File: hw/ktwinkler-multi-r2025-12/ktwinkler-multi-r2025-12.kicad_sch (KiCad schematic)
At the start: 21 parts, among them J1 USB_C_Receptacle_USB2.0_16P, J2 Conn_01x03, J3 Conn_01x03, J4 Conn_01x01, J5 Conn_01x01, SW5 MODE, U1 TPS631000DRLR, U2 LK116, U3 ESP32-C3FH4, Y1 40M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

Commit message: make a v2 idea, mroe experiments, less product...
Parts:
- removed AE1: Antenna_Dipole, symbol Device:Antenna_Dipole
- removed C1, C2, C3, C4, C5: 100nF, Capacitor_SMD:C_0603_1608Metric, symbol karl-atomic-basic:KC0603_100nF
- removed J1: USB_C_Receptacle_USB2.0_16P, Connector_USB:USB_C_Receptacle_GCT_USB4110, symbol Connector:USB_C_Receptacle_USB2.0_16P
- removed J2: Conn_01x03, Connector_PinHeader_2.54mm:PinHeader_1x03_P2.54mm_Vertical, symbol Connector_Generic:Conn_01x03
- removed J3: Conn_01x03, TerminalBlock_Phoenix_MPT-0,5-3-2.54_1x03_P2.54mm_Horizontal, symbol Connector_Generic:Conn_01x03
- removed J4, J5: Conn_01x01, Connector_Wire:SolderWire-0.5sqmm_1x01_D0.9mm_OD2.1mm, symbol Connector_Generic:Conn_01x01
- removed L1: 1uH, Inductor_SMD:L_1206_3216Metric, symbol Device:L_Small
- removed R1, R2: 5k1, Resistor_SMD:R_0603_1608Metric, symbol karl-atomic-basic:KR0603_5k1
- removed R3: 0R, Resistor_SMD:R_0603_1608Metric, symbol karl-atomic-basic:KR0603_0R
- removed U1: TPS631000DRLR, Package_TO_SOT_SMD:SOT-583-8, symbol karl-parts:TPS631000DRLR
- removed U2: LK116, Package_TO_SOT_SMD:SOT-23-6, symbol karl-parts:LK116
- removed U3: ESP32-C3FH4, Package_DFN_QFN:QFN-32-1EP_5x5mm_P0.5mm_EP3.7x3.7mm, symbol karl-parts:ESP32-C3FH4
- removed Y1: 40M, Crystal:Crystal_SMD_2016-4Pin_2.0x1.6mm, symbol Device:Crystal_GND24_Small
- removed Y2: X1A0001210005, Crystal:Crystal_SMD_MicroCrystal_CM9V-T1A-2Pin_1.6x1.0mm, symbol karl-parts:X1A0001210005
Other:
- added sheet esp32 (esp32.kicad_sch)
- added sheet leds (leds.kicad_sch)
- added sheet power (power.kicad_sch)
- note removed: "2/3 cells AA, with shitty 1.2V nimh, flat, we need buck boost from ~2V to ~4.6V Decent parts on JLC, under $0.60, with >1A RT6150A (0.8A, 1MHz) TPS63802DLAR 3A, promises 0.47uH tiny L TPS63020 4A, 2.4MHz (bigger package) TPS631000 (great stock, looks good)"
- note removed: "2016 is the cheapest smallest 40M crystal if you do this yourself the hard way Do we _realllllly_ need a 32k? yeahhhh, that's the point right?"
- note removed: "Constraints * Only the one user facing button from external * Updates? * Programming? USB-C inside? just serial pads?"
- note removed: "ESP32x in 13.2x16.6mm modules: ESP32-C6-MINI-1-N4 - well stocked, $4 (wifi+btle+802.15.4) ESP32-C61-MINI-1 - no stock ESP32-C3-MINI-1-H4X - well stocked, $3 (wifi+btle) ESP8684-MINI-1-H4 - some stock, $2 (wifi+btle) ESP32-H2-MINI-1 - no stock (btle+802.15.4 only) ESP32-PICO-MINI-02-N8R2 - well stocked, $5 (wifi+bt+btle) So... C6 or C3? fuck matter... C3 is fine :) So.. C6 has the low power coproc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"
- note removed: "Separate because these are battery contacts in the replacement board"
- note removed: "TODO: use 0402 TODO: will a vert mount fit? (prb too tall?)"
- note removed: "This controller _will_ drain the batteries when "off"! Original parts use ~370nA when "off" we'll never get that low!"
- note removed: "battery: Keystone 5201 is spring, would need bending and insertion. one of my boards is positive on left pin, one is negative.... Keystone 5223 is the other side. (on lcsc, but not good for straigth soldering!) Holes for mounting: they're in different places Buttons: different offsets and different sides!"
- note removed: "~4V, peak power is.... what? 0.4 2W? Connect the boards up again?"
- moved on the sheet: SW5

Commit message: pushing onwards like a madlad
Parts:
- added R14: 10k, Resistor_SMD:R_0402_1005Metric, symbol karl-atomic-basic:KR0402_10k
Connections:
- net GND: now reaches SW5.1
- net MODE: now reaches SW5.2
- net MODE: now also R14.2
- new net +3V3: R14.1
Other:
- added sheet ch584 (ch584.kicad_sch)
- sheet esp32 ports: added MODE, PWM1, PWM2, PWM3, PWM4, PWM5, PWM6, PWM7, PWM8; removed none
- sheet leds ports: added LED1A, LED1B, LED2A, LED2B, LED3A, LED3B, LED4A, LED4B, PWR_LEDS; removed none
- note added: "Not enough PWM on CH584F ;)"
- moved on the sheet: SW5

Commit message: ready for scope creep
I think the schematic is ... mostly ok?  I need to decide how much of
the han p1 port scope creep to bother doing, or not...

I've roughyl blocked out the board, seems as good as any?
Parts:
- added JP1, JP2: KJumper_3, Connector_PinHeader_2.54mm:PinHeader_1x03_P2.54mm_Vertical, symbol karl-parts:KJumper_3
- added R11, R20: 10k, Resistor_SMD:R_0402_1005Metric, symbol karl-atomic-basic:KR0402_10k
- added SW1: RESET, Button_Switch_SMD:SW_SPST_TL3342, symbol Switch:SW_Push
- added SW2: BOOT, Button_Switch_SMD:SW_SPST_TL3342, symbol Switch:SW_Push
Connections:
- net +3V3: now also R11.1, R20.1
- net GND: now also JP1.3 (B), JP2.3 (B), SW1.1, SW2.1
- new net GBOOT: R20.2, SW2.2
- new net RESET_CH5x: JP2.2 (Comm)
- new net RESET_ESP: JP1.2 (Comm)
- new net RESET_GLOBAL: JP1.1 (A), JP2.1 (A), R11.2, SW1.2
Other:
- added sheet ScopeCreep (scope_creep.kicad_sch)
- note added: "Lower: held in reset Upper: button controlled Both open, reset floats..."

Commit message: this is just getting silly
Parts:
- added H1, H2: Mounting_SMTSO3015CTJ, jlc-extras:Mounting_SMTSO_M3, symbol karl-parts:Mounting_SMTSO3015CTJ
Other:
- sheet ScopeCreep ports: added P1_OUT; removed none
- sheet ch584 ports: added P1IN; removed none
- sheet esp32 ports: added P1IN; removed none

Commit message: "schematic complete" (lol)
but yeah, i think this is most of it?  time to maybe route shit?
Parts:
- H1, H2: now in the parts list
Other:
- sheet ScopeCreep ports: added P1_Do_Request; removed none
- sheet ch584 ports: added P1_Req_Out; removed none
- sheet esp32 ports: added P1_Req_Out; removed none
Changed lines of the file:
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@@
+	)
+	(junction
+		(at 210.82 134.62)
+		(diameter 0)
+		(color 0 0 0 0)
 	)
 	(junction
@@
 	(wire
 		(pts
-			(xy 208.28 90.17) (xy 208.28 132.08)
+			(xy 208.28 91.44) (xy 208.28 132.08)
+		)
+		(stroke
+			(width 0)
+			(type default)
+		)
+	)
+	(wire
+		(pts
+			(xy 210.82 88.9) (xy 210.82 134.62)
 		)
 		(stroke
@@
 	(wire
 		(pts
-			(xy 177.8 90.17) (xy 208.28 90.17)
+			(xy 177.8 91.44) (xy 208.28 91.44)
 		)
 		(stroke
@@
 	(wire
 		(pts
+			(xy 177.8 88.9) (xy 210.82 88.9)
+		)
+		(stroke
+			(width 0)
+			(type default)
+		)
+	)
+	(wire
+		(pts
 			(xy 190.5 134.62) (xy 190.5 68.58)
 		)
@@
 	(wire
 		(pts
+			(xy 177.8 147.32) (xy 210.82 147.32)
+		)
+		(stroke
+			(width 0)
+			(type default)
+		)
+	)
+	(wire
+		(pts
 			(xy 50.8 162.56) (xy 50.8 165.1)
 		)
@@
 	(wire
 		(pts
+			(xy 210.82 147.32) (xy 210.82 134.62)
+		)
+		(stroke
+			(width 0)
+			(type default)
+		)
+	)
+	(wire
+		(pts
 			(xy 187.96 66.04) (xy 213.36 66.04)
 		)
@@
 		(pts
 			(xy 177.8 139.7) (xy 195.58 139.7)
+		)
+		(stroke
+			(width 0)
+			(type default)
+		)
+	)
+	(wire
+		(pts
+			(xy 210.82 134.62) (xy 220.98 134.62)
 		)
 		(stroke
@@
 		(unit 1)
 		(exclude_from_sim no)
-		(in_bom no)
+		(in_bom yes)
 		(on_board yes)
 		(dnp no)
@@
 		(unit 1)
 		(exclude_from_sim no)
-		(in_bom no)
+		(in_bom yes)
 		(on_board yes)
 		(dnp no)
@@
 			)
 		)
+		(pin "P1_Req_Out" output
+			(at 177.8 147.32 0)
+			(effects
+				(font
+					(size 1.27 1.27)
+				)
+				(justify right)
+			)
+		)
 		(instances
 			(project "ktwinkler-multi-r2025-12"
@@
 			)
 		)
+		(pin "P1_Do_Request" input
+			(at 220.98 134.62 180)
+			(effects
+				(font
+					(size 1.27 1.27)
+				)
+				(justify left)
+			)
+		)
 		(instances
 			(project "ktwinkler-multi-r2025-12"
@@
 		)
 		(pin "P1IN" input
-			(at 177.8 90.17 0)
-			(effects
-				(font
+			(at 177.8 91.44 0)
+			(effects
+				(font
+					(size 1.27 1.27)
+				)
+				(justify right)
+			)
+		)
+		(pin "P1_Req_Out" output
+			(at 177.8 88.9 0)
+			(effects
+				(font

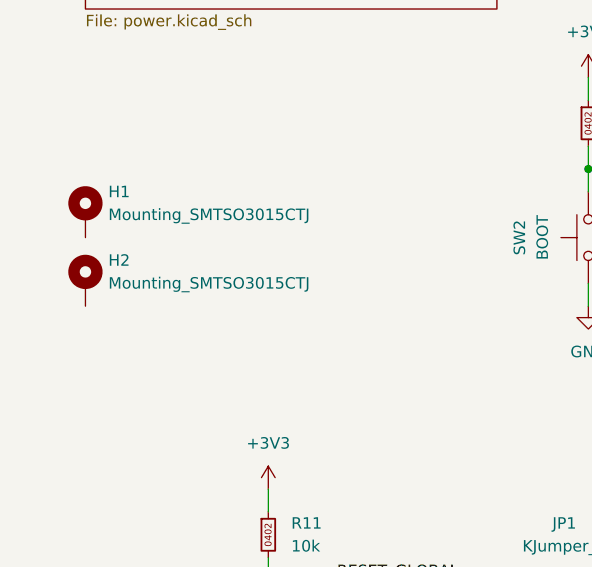
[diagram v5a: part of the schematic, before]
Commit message: update following ERC and symbol fixes
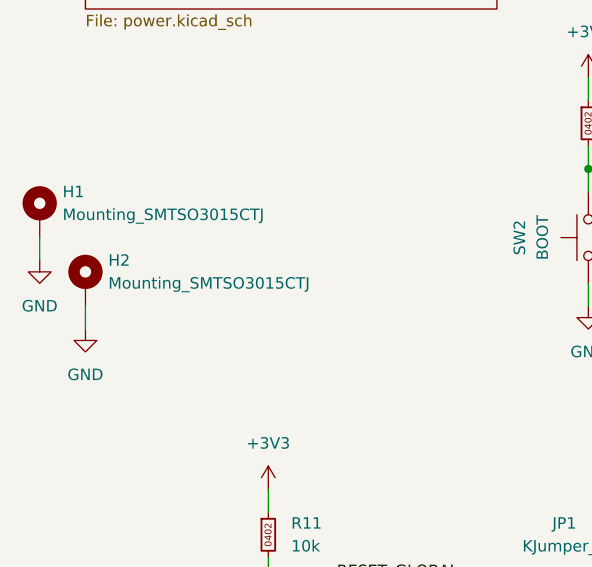
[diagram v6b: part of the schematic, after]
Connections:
- net GND: now also H1.1, H2.1
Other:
- moved on the sheet: H1
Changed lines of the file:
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@@
+	(wire
+		(pts
+			(xy 25.4 127) (xy 25.4 129.54)
+		)
+		(stroke
+			(width 0)
+			(type default)
+		)
+	)
 	(wire
 		(pts
@@
 		(pts
 			(xy 50.8 177.8) (xy 50.8 180.34)
+		)
+		(stroke
+			(width 0)
+			(type default)
+		)
+	)
+	(wire
+		(pts
+			(xy 30.48 134.62) (xy 30.48 137.16)
 		)
 		(stroke
@@
 	(symbol
 		(lib_id "power:GND")
+		(at 25.4 129.54 0)
+		(unit 1)
+		(exclude_from_sim no)
+		(in_bom yes)
+		(on_board yes)
+		(dnp no)
+		(fields_autoplaced yes)
+		(property "Reference" "#PWR059"
+			(at 25.4 135.89 0)
+			(effects
+				(font
+					(size 1.27 1.27)
+				)
+				(hide yes)
+			)
+		)
+		(property "Value" "GND"
+			(at 25.4 134.62 0)
+			(effects
+				(font
+					(size 1.27 1.27)
+				)
+			)
+		)
+		(property "Footprint" ""
+			(at 25.4 129.54 0)
+			(effects
+				(font
+					(size 1.27 1.27)
+				)
+				(hide yes)
+			)
+		)
+		(property "Datasheet" ""
+			(at 25.4 129.54 0)
+			(effects
+				(font
+					(size 1.27 1.27)
+				)
+				(hide yes)
+			)
+		)
+		(property "Description" "Power symbol creates a global label with name \"GND\" , ground"
+			(at 25.4 129.54 0)
+			(effects
+				(font
+					(size 1.27 1.27)
+				)
+				(hide yes)
+			)
+		)
+		(pin "1"
+		)
+		(instances
+			(project "ktwinkler-multi-r2025-12"
+				(path "/48773b41-b773-40e2-8ba4-2e78c7a3e45f"
+					(reference "#PWR059")
+					(unit 1)
+				)
+			)
+		)
+	)
+	(symbol
+		(lib_id "power:GND")
 		(at 50.8 180.34 0)
 		(unit 1)
@@
 	(symbol
 		(lib_id "karl-parts:Mounting_SMTSO3015CTJ")
-		(at 30.48 124.46 0)
+		(at 25.4 124.46 0)
 		(unit 1)
 		(exclude_from_sim no)
@@
 		(fields_autoplaced yes)
 		(property "Reference" "H1"
-			(at 33.02 121.9199 0)
+			(at 27.94 121.9199 0)
 			(effects
 				(font
@@
 		)
 		(property "Value" "Mounting_SMTSO3015CTJ"
-			(at 33.02 124.4599 0)
+			(at 27.94 124.4599 0)
 			(effects
 				(font
@@
 		)
 		(property "Footprint" "jlc-extras:Mounting_SMTSO_M3"
-			(at 30.48 124.46 0)
+			(at 25.4 124.46 0)
 			(effects
 				(font
@@
 		)
 		(property "Datasheet" "https://jlcpcb.com/api/file/downloadByFileSystemAccessId/8588954979927535616"
-			(at 30.48 124.46 0)
+			(at 25.4 124.46 0)
 			(effects
 				(font
@@
 		)
 		(property "Description" "PCB SMT nut M3x1.5mm"
-			(at 30.48 124.46 0)
+			(at 25.4 124.46 0)
 			(effects
 				(font
@@
 		)
 		(property "MPN" "SMTSO3015CTJ"
-			(at 30.48 124.46 0)
+			(at 25.4 124.46 0)
 			(effects
 				(font
@@
 		)
 		(property "jlcbasic" "0"
-			(at 30.48 124.46 0)
+			(at 25.4 124.46 0)
 			(effects
 				(font
@@
 		)
 		(property "LCSC Part #" "C2915632"
-			(at 30.48 124.46 0)
+			(at 25.4 124.46 0)
 			(effects
 				(font
@@
 					(unit 1)
 				)
+			)
+		)
+	)
+	(symbol
+		(lib_id "power:GND")
+		(at 30.48 137.16 0)
+		(unit 1)
+		(exclude_from_sim no)
+		(in_bom yes)
+		(on_board yes)
+		(dnp no)
+		(fields_autoplaced yes)
+		(property "Reference" "#PWR058"
+			(at 30.48 143.51 0)
+			(effects
+				(font
+					(size 1.27 1.27)
+				)
+				(hide yes)
+			)
+		)
+		(property "Value" "GND"
+			(at 30.48 142.24 0)
+			(effects
+				(font
+					(size 1.27 1.27)
+				)
+			)
+		)
+		(property "Footprint" ""
+			(at 30.48 137.16 0)
+			(effects
+				(font
+					(size 1.27 1.27)
+				)
+				(hide yes)
+			)
+		)
+		(property "Datasheet" ""
+			(at 30.48 137.16 0)
+			(effects
+				(font
+					(size 1.27 1.27)
+				)
+				(hide yes)
+			)
+		)
+		(property "Description" "Power symbol creates a global label with name \"GND\" , ground"
+			(at 30.48 137.16 0)
+			(effects
+				(font
+					(size 1.27 1.27)
+				)
+				(hide yes)
+			)
+		)
+		(pin "1"
+		)
+		(instances
+			(project "ktwinkler-multi-r2025-12"
+				(path "/48773b41-b773-40e2-8ba4-2e78c7a3e45f"
+					(reference "#PWR058")
+					(unit 1)
+				)

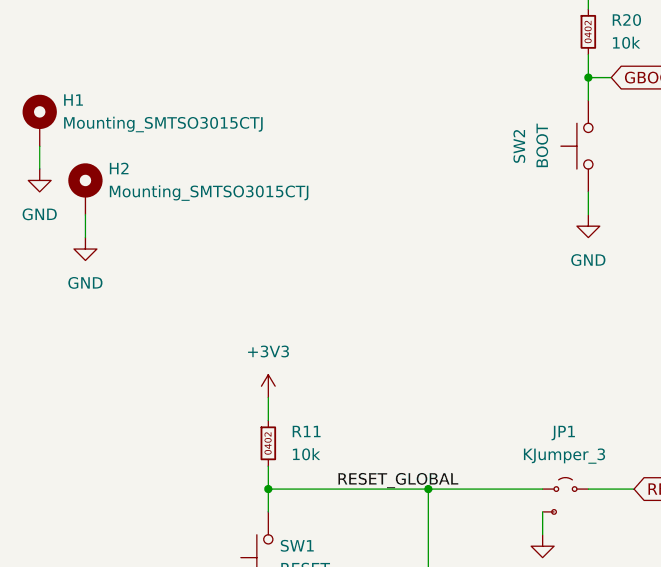
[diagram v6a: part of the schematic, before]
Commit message: streammmm updates
"complete" apart from finishing those antennas.
needs DRC cleanups on both the wch inv-f and also the yolo-pole.
need to at least _basically_ get the antenna trace basic wdith correct
as well.  yolo is fine, when it's guided yolo, not "lol"
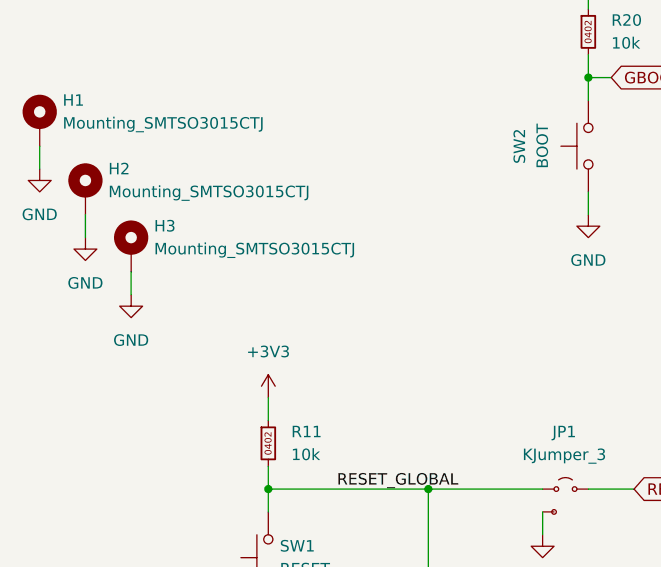
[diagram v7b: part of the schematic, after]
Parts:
- added H3: Mounting_SMTSO3015CTJ, jlc-extras:Mounting_SMTSO_M3, symbol karl-parts:Mounting_SMTSO3015CTJ
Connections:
- net GND: now also H3.1
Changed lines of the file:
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@@
+	(wire
+		(pts
+			(xy 35.56 140.97) (xy 35.56 143.51)
+		)
+		(stroke
+			(width 0)
+			(type default)
+		)
+	)
 	(wire
 		(pts
@@
 				(path "/48773b41-b773-40e2-8ba4-2e78c7a3e45f"
 					(reference "R11")
+					(unit 1)
+				)
+			)
+		)
+	)
+	(symbol
+		(lib_id "karl-parts:Mounting_SMTSO3015CTJ")
+		(at 35.56 138.43 0)
+		(unit 1)
+		(exclude_from_sim no)
+		(in_bom yes)
+		(on_board yes)
+		(dnp no)
+		(fields_autoplaced yes)
+		(property "Reference" "H3"
+			(at 38.1 135.8899 0)
+			(effects
+				(font
+					(size 1.27 1.27)
+				)
+				(justify left)
+			)
+		)
+		(property "Value" "Mounting_SMTSO3015CTJ"
+			(at 38.1 138.4299 0)
+			(effects
+				(font
+					(size 1.27 1.27)
+				)
+				(justify left)
+			)
+		)
+		(property "Footprint" "jlc-extras:Mounting_SMTSO_M3"
+			(at 35.56 138.43 0)
+			(effects
+				(font
+					(size 1.27 1.27)
+				)
+				(hide yes)
+			)
+		)
+		(property "Datasheet" "https://jlcpcb.com/api/file/downloadByFileSystemAccessId/8588954979927535616"
+			(at 35.56 138.43 0)
+			(effects
+				(font
+					(size 1.27 1.27)
+				)
+				(hide yes)
+			)
+		)
+		(property "Description" "PCB SMT nut M3x1.5mm"
+			(at 35.56 138.43 0)
+			(effects
+				(font
+					(size 1.27 1.27)
+				)
+				(hide yes)
+			)
+		)
+		(property "MPN" "SMTSO3015CTJ"
+			(at 35.56 138.43 0)
+			(effects
+				(font
+					(size 1.27 1.27)
+				)
+				(hide yes)
+			)
+		)
+		(property "jlcbasic" "0"
+			(at 35.56 138.43 0)
+			(effects
+				(font
+					(size 1.27 1.27)
+				)
+				(hide yes)
+			)
+		)
+		(property "LCSC Part #" "C2915632"
+			(at 35.56 138.43 0)
+			(effects
+				(font
+					(size 1.27 1.27)
+				)
+				(hide yes)
+			)
+		)
+		(pin "1"
+		)
+		(instances
+			(project "ktwinkler-multi-r2025-12"
+				(path "/48773b41-b773-40e2-8ba4-2e78c7a3e45f"
+					(reference "H3")
 					(unit 1)
 				)
@@
 					(unit 1)
 				)
+			)
+		)
+	)
+	(symbol
+		(lib_id "power:GND")
+		(at 35.56 143.51 0)
+		(unit 1)
+		(exclude_from_sim no)
+		(in_bom yes)
+		(on_board yes)
+		(dnp no)
+		(fields_autoplaced yes)
+		(property "Reference" "#PWR060"
+			(at 35.56 149.86 0)
+			(effects
+				(font
+					(size 1.27 1.27)
+				)
+				(hide yes)
+			)
+		)
+		(property "Value" "GND"
+			(at 35.56 148.59 0)
+			(effects
+				(font
+					(size 1.27 1.27)
+				)
+			)
+		)
+		(property "Footprint" ""
+			(at 35.56 143.51 0)
+			(effects
+				(font
+					(size 1.27 1.27)
+				)
+				(hide yes)
+			)
+		)
+		(property "Datasheet" ""
+			(at 35.56 143.51 0)
+			(effects
+				(font
+					(size 1.27 1.27)
+				)
+				(hide yes)
+			)
+		)
+		(property "Description" "Power symbol creates a global label with name \"GND\" , ground"
+			(at 35.56 143.51 0)
+			(effects
+				(font
+					(size 1.27 1.27)
+				)
+				(hide yes)
+			)
+		)
+		(pin "1"
+		)
+		(instances
+			(project "ktwinkler-multi-r2025-12"
+				(path "/48773b41-b773-40e2-8ba4-2e78c7a3e45f"
+					(reference "#PWR060")
+					(unit 1)
+				)

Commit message: attempting to progres towards a build
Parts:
- H1, H2, H3: footprint jlc-extras:Mounting_SMTSO_M3 -> jlc-extras:Mounting_SMTSO_M3_ALT
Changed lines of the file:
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@@
 			)
 		)
-		(property "Footprint" "jlc-extras:Mounting_SMTSO_M3"
+		(property "Footprint" "jlc-extras:Mounting_SMTSO_M3_ALT"
 			(at 35.56 138.43 0)
 			(effects
@@
 			)
 		)
-		(property "Footprint" "jlc-extras:Mounting_SMTSO_M3"
+		(property "Footprint" "jlc-extras:Mounting_SMTSO_M3_ALT"
 			(at 30.48 132.08 0)
 			(effects
@@
 			)
 		)
-		(property "Footprint" "jlc-extras:Mounting_SMTSO_M3"
+		(property "Footprint" "jlc-extras:Mounting_SMTSO_M3_ALT"
 			(at 25.4 124.46 0)
 			(effects
